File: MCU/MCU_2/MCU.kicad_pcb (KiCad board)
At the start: 4 copper layers, 100 x 100 mm, 245 parts, among them J10 RotEnc, J11 In Relay, J12 Out Relay, J13 ALC out, J14 Conn_01x02, J15 Conn_01x02, J16 Conn_01x02, J17 Conn_01x04, J18 Conn_01x02, J19 RF, J2 Conn_01x08, J20 CAN, J21 Conn_01x04, J22 12Vin, J23 BIAS, J3 Conn_02x20_Odd_Even, J4 SWD, J5 PowerSense, J6 NTC1, J7 NTC2, J8 SWR1, J9 SWR2, M1 Fan, M2 Fan, Q1 DTC144E, Q10 AO3402, Q11 AO3402, Q12 DTC144E, Q13 DTA144E, Q14 DTA124E, Q15 DTC124E, Q16 2N5401, Q17 DTC144E, Q18 DTA144E, Q19 DTA144E, Q2 8050, Q3 8050, Q4 DTC144E, Q5 DTA144E, Q6 DTC144E, Q7 DTC144E, Q8 DTA144E, Q9 DTA144E, SW1 SW_DIP_x04, U1 74HC04, U10 MT2492/SY8120, U11 PC817, U12 TL431, U13 AZ1117-3.3, U14 AZ1117-3.3, U15 LMV321, U16 MAX3232, U17 TJA1042T, U2 STM32F407VETx, U3 LMV358, U4 LMV324, U5 LMV358, U6 LMV324, U7 LMV324, U8 TLC555xD, U9 ICL7660, Y1 12MHz

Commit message: MCU PCB start layouting
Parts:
- removed C37: 103, lc_lib:0805_C
- removed C47: 104, lc_lib:0805_C
- removed D15: 16V, lc_lib:SMA(DO-214AC)_S4
- removed FB3: 1K, lc_lib:0805_R
- removed J16: Conn_01x02, Connector_PinHeader_2.54mm:PinHeader_1x02_P2.54mm_Vertical
- removed JP1: 0, lc_lib:0805_R
- removed L4: BEAD, lc_lib:1206_L
- added C68: 10uF, lc_lib:0805_C, B.Cu at (43.6, 44.5)
- C42: footprint Capacitor_THT:CP_Radial_D5.0mm_P2.50mm -> lc_lib:0805_C
- C48: value 104 -> 10uF
- C63: value 10V 100uF -> 10uF; footprint Capacitor_THT:CP_Radial_D5.0mm_P2.50mm -> lc_lib:0805_C
- J14: value Conn_01x02 -> TX_GND
- J15: value Conn_01x02 -> SW
- J17: value Conn_01x04 -> COM
- J18: value Conn_01x02 -> BAND
- J2: value Conn_01x08 -> LPF
- J21: value Conn_01x04 -> COM_R
- L5: value 10uH -> 6.8uH
- moved L2 376.6 mm to (175.1, 79.4)
- moved L3 370.4 mm to (168.1, 79.4)
- moved U1 357.5 mm to (178.8, 69.8)
- moved J18 328.6 mm to (106.0, 23.0), turned to 270 degrees
- moved J14 322.3 mm to (92.0, 23.0), turned to 270 degrees
- moved J15 318.4 mm to (85.0, 23.0), turned to 270 degrees
- moved J13 305.0 mm to (99.0, 23.0), turned to 270 degrees
- moved C43 286.7 mm to (34.1, 39.0), turned to 180 degrees
- moved D9 286.1 mm to (78.0, 34.0), turned to 270 degrees
- moved C9 281.5 mm to (-45.1, 9.65)
- moved R59 279.8 mm to (51.9, 51.0), turned to 180 degrees
- moved U12 278.9 mm to (47.0, 48.5), turned to 270 degrees
- moved R2 276.5 mm to (51.9, 47.5)
- moved C11 275.7 mm to (-44.9, 17.3)
- moved R8 274.5 mm to (-36.0, 9.65)
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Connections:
- C41 pad 1: Net-(C41-Pad1) -> +12V
- C42 pad 1: Net-(C41-Pad1) -> +12V
- J15 pad 1: GND -> Net-(D12-Pad2)
- J15 pad 2: Net-(D12-Pad2) -> GND
- R63 pad 1: Net-(C41-Pad1) -> +12V
- U10 pad 5: Net-(C41-Pad1) -> +12V

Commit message: routing signals
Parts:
- removed J18: BAND, Connector_PinHeader_2.54mm:PinHeader_1x02_P2.54mm_Vertical
- removed L2, L3, L6, L7: 600Ohm, lc_lib:0805_L
- removed R62: 100, lc_lib:0805_R
- removed R72: 1K, lc_lib:0805_R
- removed U15: LMV321, lc_lib:SOT-23-5
- added C37: 104, lc_lib:0805_C, B.Cu at (56.8, 85.2)
- added C47: 104, lc_lib:0805_C, B.Cu at (66.8, 50.0)
- added C69: 104, lc_lib:0805_C, B.Cu at (71.4, 54.2)
- C1, C2: value C_Small -> 20
- C22, C23: value C_Small -> 104
- FB7: footprint lc_lib:1206_R -> lc_lib:0201_R
- J20: footprint Connector_JST:JST_PH_B2B-PH-SM4-TB_1x02-1MP_P2.00mm_Vertical -> Connector_PinHeader_2.54mm:PinHeader_1x02_P2.54mm_Vertical
- J4: footprint Connector_JST:JST_PH_B4B-PH-SM4-TB_1x04-1MP_P2.00mm_Vertical -> Connector_PinHeader_2.54mm:PinHeader_1x04_P2.54mm_Vertical
- SW1: footprint lc_lib:DIP-8 -> Button_Switch_SMD:SW_DIP_SPSTx04_Slide_KingTek_DSHP04TS_W7.62mm_P1.27mm
- moved R40 178.8 mm to (107.5, 49.7)
- moved R20 176.0 mm to (107.0, 39.0)
- moved R7 176.0 mm to (109.5, 101.6), turned to 180 degrees
- moved C23 175.3 mm to (99.0, 66.2), turned to 90 degrees
- moved R8 173.9 mm to (109.5, 104.8), turned to 180 degrees
- moved R21 172.5 mm to (103.2, 47.4), turned to 90 degrees
- moved R26 170.3 mm to (107.6, 53.0), turned to 180 degrees
- moved U5 170.2 mm to (89.4, 54.4)
- moved R18 170.2 mm to (107.0, 35.6)
- moved R33 170.1 mm to (107.2, 93.8), turned to 180 degrees
- moved U3 167.8 mm to (102.0, 39.5)
- moved U6 167.7 mm to (99.0, 90.8)
- moved R39 167.0 mm to (107.2, 61.2)
- moved R32 166.4 mm to (107.2, 90.5), turned to 180 degrees
- moved R9 165.3 mm to (109.5, 107.8)
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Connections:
- C1 pad 2: GNDD -> GND
- C10 pad 2: GND -> GNDA
- C11 pad 2: GND -> GNDA
- C12 pad 1: GND -> GNDA
- C13 pad 2: GND -> GNDA
- C14 pad 2: GND -> GNDA
- C15 pad 2: GND -> GNDA
- C16 pad 1: GND -> GNDA
- C17 pad 2: GND -> GNDA
- C18 pad 1: GND -> GNDA
- C19 pad 2: GND -> GNDA
- C2 pad 2: GNDD -> GND
- C20 pad 2: GND -> GNDA
- C21 pad 2: GND -> GNDA
- C22 pad 2: GND -> GNDA
- C23 pad 2: GND -> GNDA
- C24 pad 2: GND -> GNDA
- C25 pad 2: GND -> GNDA
- C26 pad 2: GND -> GNDA
- C27 pad 2: GND -> GNDA
- C28 pad 2: GND -> GNDA
- C29 pad 2: GND -> GNDA
- C3 pad 2: GNDD -> GND
- C30 pad 2: GND -> GNDA
- C31 pad 2: GND -> GNDA
- C34 pad 2: GNDD -> GND
- C38 pad 2: GND -> GNDA
- C4 pad 2: GNDD -> GND
- C40 pad 1: GND -> +3V3
- C40 pad 2: Net-(C40-Pad2) -> GND
- C5 pad 1: +3V3 -> GND
- C5 pad 2: GNDD -> Net-(C5-Pad2)
- C53 pad 2: GNDD -> GND
- C55 pad 1: GNDD -> GND
- C57 pad 2: GNDD -> GND
- C58 pad 2: GNDD -> GND
- C59 pad 2: GND -> GNDA
- C6 pad 2: GNDD -> GND
- C65 pad 2: GND -> GNDA
- C7 pad 2: GNDD -> GND
- C8 pad 2: GNDD -> GND
- C9 pad 2: GNDD -> GND
- D16 pad 1: Net-(D16-Pad1) -> GND
- FB7 pad 1: GND -> GNDA
- FB7 pad 2: GNDD -> GND
- J17 pad 4: GNDD -> GND
- J19 pad 8: GND -> GNDA
- J20 pad 1: CAN- -> CAN+
- J20 pad 2: CAN+ -> CAN-
- J21 pad 4: GNDD -> GND
- J3 pad 1: GNDD -> GND
- J3 pad 40: GNDD -> GND
- J4 pad 4: GNDD -> GND
- J5 pad 4: GND -> GNDA
- J8 pad 1: GND -> +5V
- J8 pad 2: REV1 -> FWDpeak1
- J8 pad 3: REVpeak1 -> FWD1
- J8 pad 4: FWD1 -> REVpeak1
- J8 pad 5: FWDpeak1 -> REV1
- J8 pad 6: +5V -> GNDA
- J9 pad 1: GND -> +5V
- J9 pad 2: REV2 -> FWDpeak2
- J9 pad 3: REVpeak2 -> FWD2
- J9 pad 4: FWD2 -> REVpeak2
- J9 pad 5: FWDpeak2 -> REV2
- J9 pad 6: +5V -> GNDA
- Q1 pad 2: GND -> GNDA
- Q13 pad 3: GNDD -> GND
- Q15 pad 2: GNDD -> GND
- Q4 pad 2: GND -> GNDA
- Q6 pad 2: GND -> GNDA
- Q7 pad 2: GND -> GNDA
- R13 pad 2: GNDD -> GND
- R20 pad 1: GND -> GNDA
- R22 pad 1: GND -> GNDA
- R25 pad 1: GND -> GNDA
- R30 pad 1: GND -> GNDA
- R39 pad 1: GND -> GNDA
- R40 pad 1: GND -> GNDA
- R53 pad 1: GND -> GNDA
- R80 pad 2: +5V -> +5VA
- U16 pad 15: GNDD -> GND
- U2 pad 10: GNDD -> GND
- U2 pad 20: GND -> GNDA
- U2 pad 27: GNDD -> GND
- U2 pad 47: Net-(L6-Pad2) -> /TX3
- U2 pad 48: Net-(L7-Pad1) -> /RX3
- U2 pad 65: \Fatal -> Net-(U2-Pad65)
- U2 pad 68: Net-(L2-Pad2) -> /TX
- U2 pad 69: Net-(L3-Pad2) -> /RX
- U2 pad 74: GNDD -> GND
- U2 pad 87: Net-(U2-Pad87) -> \Fatal
- U2 pad 99: GNDD -> GND
- U3 pad 4: GND -> GNDA
- U4 pad 11: GND -> GNDA
- U5 pad 4: GND -> GNDA
- U6 pad 11: GND -> GNDA
- U7 pad 11: GND -> GNDA
- U8 pad 5: Net-(U8-Pad5) -> Net-(C5-Pad2)
- Y1 pad 2: GNDD -> GND
- Y1 pad 4: GNDD -> GND
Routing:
- net +3V3: track 0.00 -> 148.6 mm, vias 0 -> 36
- net /ADC1_9: track 0.00 -> 128.3 mm, vias 0 -> 8
- net /ExternalInput/PTT_RTS: track 0.00 -> 123.2 mm, vias 0 -> 8
- net \Fatal: track 0.00 -> 107.8 mm, vias 0 -> 7
- net /ADC3_10: track 0.00 -> 89.8 mm, vias 0 -> 4
- net /ADC3_11: track 0.00 -> 88.6 mm, vias 0 -> 4
- net /ADC3_12: track 0.00 -> 80.3 mm, vias 0 -> 6
- net PWR_on_sig: track 0.00 -> 78.9 mm, vias 0 -> 3
- net +12V: track 0.00 -> 78.1 mm, vias 0 -> 1
- net /ADC3_13: track 0.00 -> 75.3 mm, vias 0 -> 4
- net /ADC1_7: track 0.00 -> 72.1 mm, vias 0 -> 2
- net /ADC1_5: track 0.00 -> 71.9 mm, vias 0 -> 2
- net /ADC1_3: track 0.00 -> 70.5 mm, vias 0 -> 2
- net \Im_HIGH: track 0.00 -> 70.2 mm, vias 0 -> 7
- net /ADC1_6: track 0.00 -> 68.2 mm, vias 0 -> 2
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- added copper zone on B.Cu, net +5V
- added copper zone on B.Cu, net GND
- added copper zone on B.Cu, net Net-(C43-Pad1)
- added copper zone on B.Cu, net Net-(C43-Pad2)

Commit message: almost finished routing MCU2
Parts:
- added R5: 0, lc_lib:0603_R, B.Cu at (38.8, 85.5)
- FB7: moved to F.Cu
- moved FB7 20.9 mm to (34.0, 30.0)
- moved F1 15.6 mm to (40.8, 24.2)
- moved C44 11.2 mm to (26.2, 31.0), turned to 180 degrees
- moved R68 7.40 mm to (22.6, 31.8)
- moved R63 6.99 mm to (39.8, 38.0)
- moved R67 3.01 mm to (30.4, 31.0), turned to 0 degrees
- moved D8 2.80 mm to (40.8, 29.6), turned to 270 degrees
- moved J22 1.00 mm to (34.0, 26.0), turned to 180 degrees
- moved C61 0.56 mm to (45.5, 31.5)
- moved R54 0.56 mm to (49.8, 31.5)
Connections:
- C19 pad 1: +5V -> +5VA
- C21 pad 1: +5V -> +5VA
- J8 pad 1: +5V -> +5VA
- J9 pad 1: +5V -> +5VA
- U2 pad 8: AUTO_BAND -> PwrOnSig
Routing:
- net GNDA: track 60.7 -> 421.6 mm, vias 44 -> 49
- net +5VA: track 34.0 -> 296.9 mm, vias 1 -> 5
- net +12V: track 78.1 -> 295.3 mm, vias 1 -> 14
- net /RX: track 10.3 -> 88.2 mm, vias 2 -> 6
- net /TX: track 8.48 -> 84.5 mm, vias 2 -> 6
- net \SpareSig: track 2.36 -> 70.1 mm, vias 0 -> 4
- net /ENC_A: track 3.31 -> 60.2 mm, vias 0 -> 2
- net /ENC_SW: track 2.47 -> 59.4 mm, vias 0 -> 4
- net PwrOnSig: track 0.00 -> 56.6 mm, vias 0 -> 4
- net /ENC_B: track 2.47 -> 56.1 mm, vias 0 -> 2
- net GND: track 65.4 -> 112.7 mm, vias 50 -> 127
- net VREF: track 11.2 -> 51.1 mm, vias 0 -> 2
- net +3V3: track 148.6 -> 184.6 mm, vias 36 -> 51
- net Net-(C65-Pad1): track 6.57 -> 38.8 mm, vias 0 -> 2
- net ALC: track 9.25 -> 33.9 mm, vias 0 -> 2
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- added copper zone on B.Cu, net +12V
- added copper zone on In1.Cu, net +3V3
- added copper zone on In2.Cu, net GND

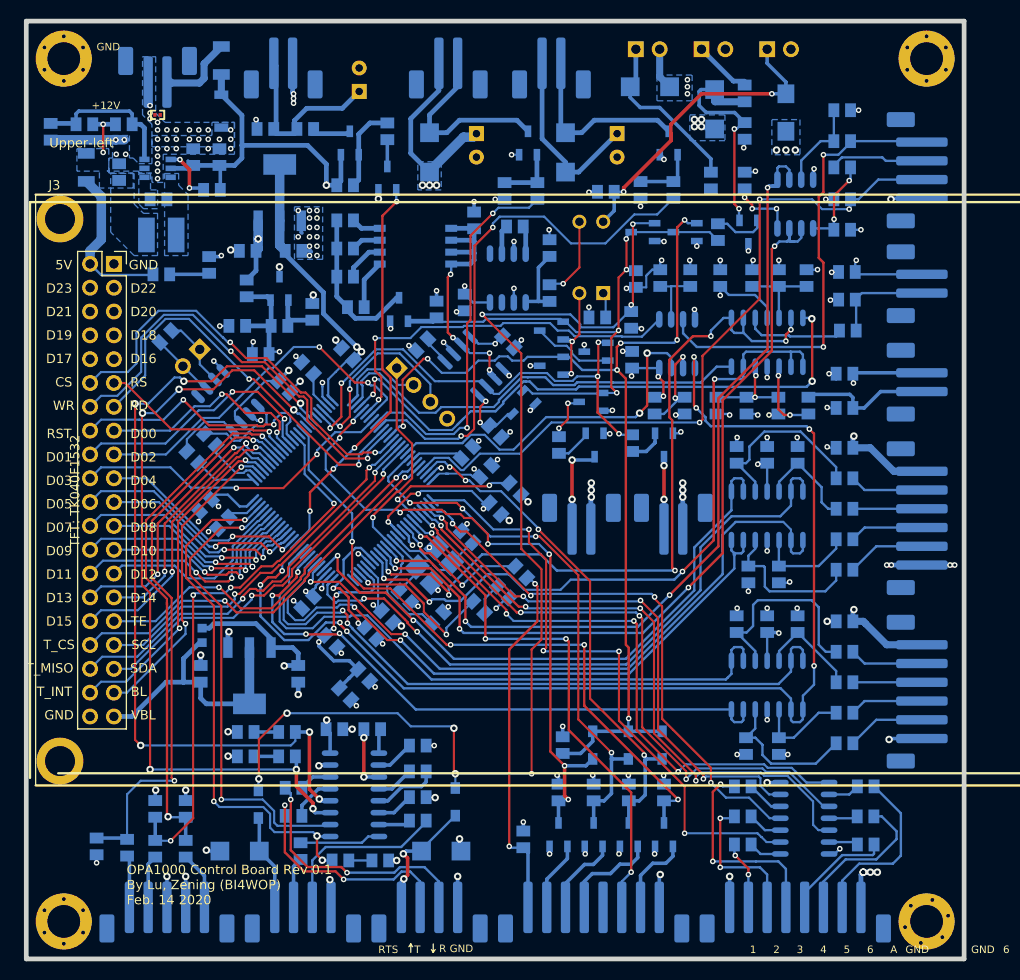
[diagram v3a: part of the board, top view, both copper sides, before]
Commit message: added EEPROM to MCU
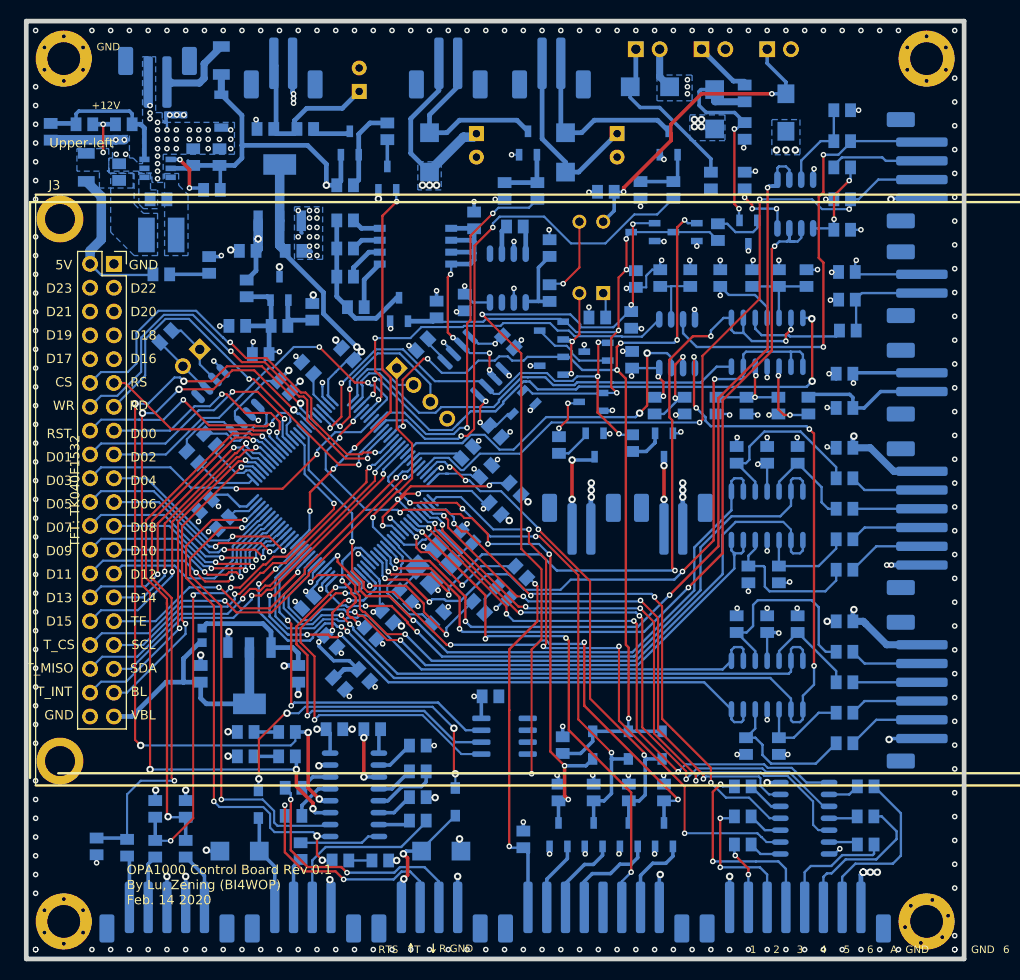
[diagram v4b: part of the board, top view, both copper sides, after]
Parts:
- added C70: 104, lc_lib:0805_C, B.Cu at (69.5, 92.0)
- added U15: M24C02-FMN, Package_SO:SOIC-8_3.9x4.9mm_P1.27mm, B.Cu at (71.0, 96.2)
- C57, C58: value 104 -> 2.2uF
- FB7: moved to B.Cu
- J23: value BIAS -> RF_12V
- moved L1 1.29 mm to (53.4, 90.6)
- moved FB7 1.03 mm to (34.9, 30.5), turned to 270 degrees
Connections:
- Q17 pad 1: BIAS_ON -> RF_12V_ON
- U2 pad 24: /ADC3_1 -> /EEP_SDA
- U2 pad 25: Net-(U2-Pad25) -> /EEP_SCL
- U2 pad 34: Net-(U2-Pad34) -> /EEP_WP
- U2 pad 37: BIAS_ON -> RF_12_ON
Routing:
- net /EEP_WP: track 0.00 -> 40.2 mm, vias 0 -> 2
- net /EEP_SDA: track 0.00 -> 39.9 mm, vias 0 -> 2
- net /EEP_SCL: track 0.00 -> 38.2 mm, vias 0 -> 2
- net GNDA: track 421.6 -> 403.4 mm, vias 49 -> 50
- net +3V3: track 184.6 -> 187.1 mm, vias 51 -> 52
- net /ADC1_7: track 71.9 -> 69.4 mm
- net GND: track 112.7 -> 114.6 mm, vias 127 -> 299
- net /ADC1_6: track 68.2 -> 66.6 mm
- net Net-(J2-Pad5): track 11.7 -> 13.0 mm
- net /ADC1_8: track 66.0 -> 64.8 mm
- net /X1: track 10.9 -> 12.1 mm
- net /ADC1_5: track 71.2 -> 72.4 mm
- net /ADC1_3: track 69.7 -> 68.7 mm
- net VREF: track 51.1 -> 52.0 mm
- net /ADC1_4: track 64.7 -> 64.0 mm
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- added copper zone on F.Cu, net GND
- added copper zone on In1.Cu, net GND
- added copper zone on B.Cu, net GNDA
